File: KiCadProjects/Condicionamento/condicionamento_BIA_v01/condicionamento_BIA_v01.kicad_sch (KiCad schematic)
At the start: 33 parts, among them J2 tensoes, J3 sinais analogicos, J4 comunicacao / sinais digitais, U1 AD828AN, U2 AD828AN

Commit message: mudanças circuito de condicionamento
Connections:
- net +9V: now also U1.8 (V+), U2.8 (V+)
- net -9V: now also U1.4 (V-), U2.4 (V-)
- net Ampl1: now also U1.3 (+IN1), U2.3 (+IN1)
- net Ampl1_medida: now reaches C1.1, D1.2 (A), D2.1 (K), R1.2
- net Ampl1_medida: now also C2.1, D3.2 (A), D4.1 (K), R2.2
- net E1: now reaches U2.5 (+IN2)
- net E1: now also J3.1 (Pin_1)
- net E1_condicionado: now reaches C8.1, D7.2 (A), D8.1 (K), R12.2
- net E1_condicionado: now also J3.3 (Pin_3)
- net E2: now reaches J3.2 (Pin_2)
- net E2: now also U1.5 (+IN2)
- net E2_condicionado: now reaches J3.4 (Pin_4)
- net E2_condicionado: now also C7.1, D5.2 (A), D6.1 (K), R11.2
- removed net +12V: J2.2 (Pin_2), U1.8 (V+), U2.8 (V+)
- removed net -12V: J2.3 (Pin_3), U1.4 (V-), U2.4 (V-)
- new net VCC: J2.2 (Pin_2)
- new net VEE: J2.3 (Pin_3)

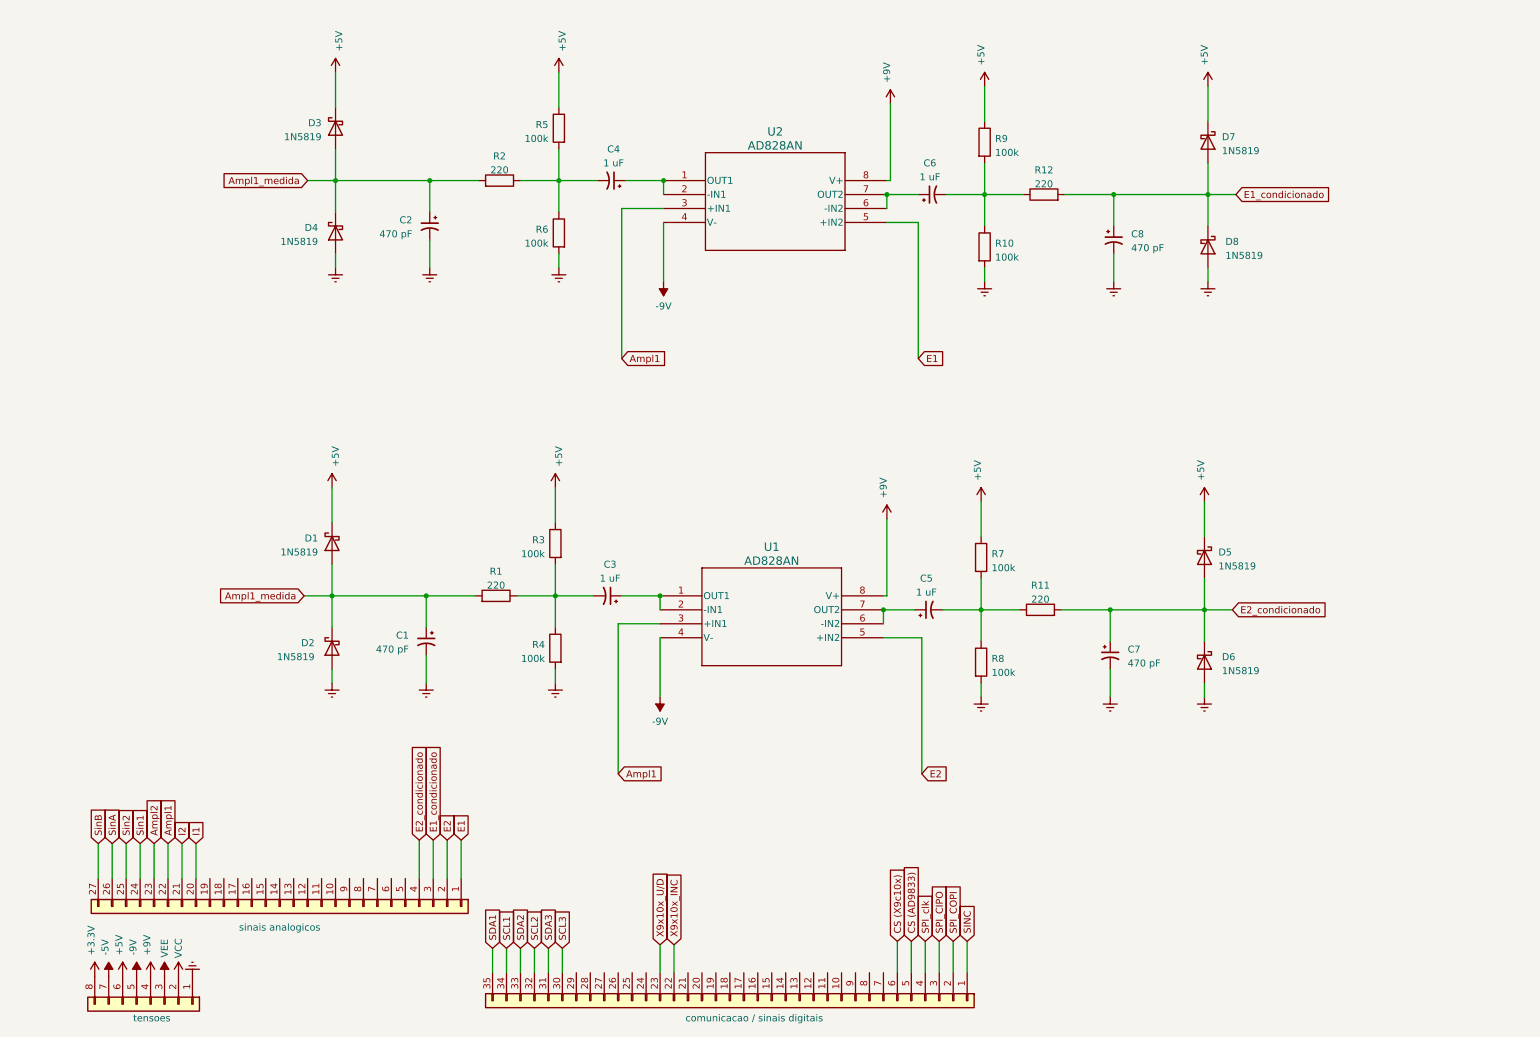
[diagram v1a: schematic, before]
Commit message: modificação: pinos de Vref para escolha da tensao de condicionamento
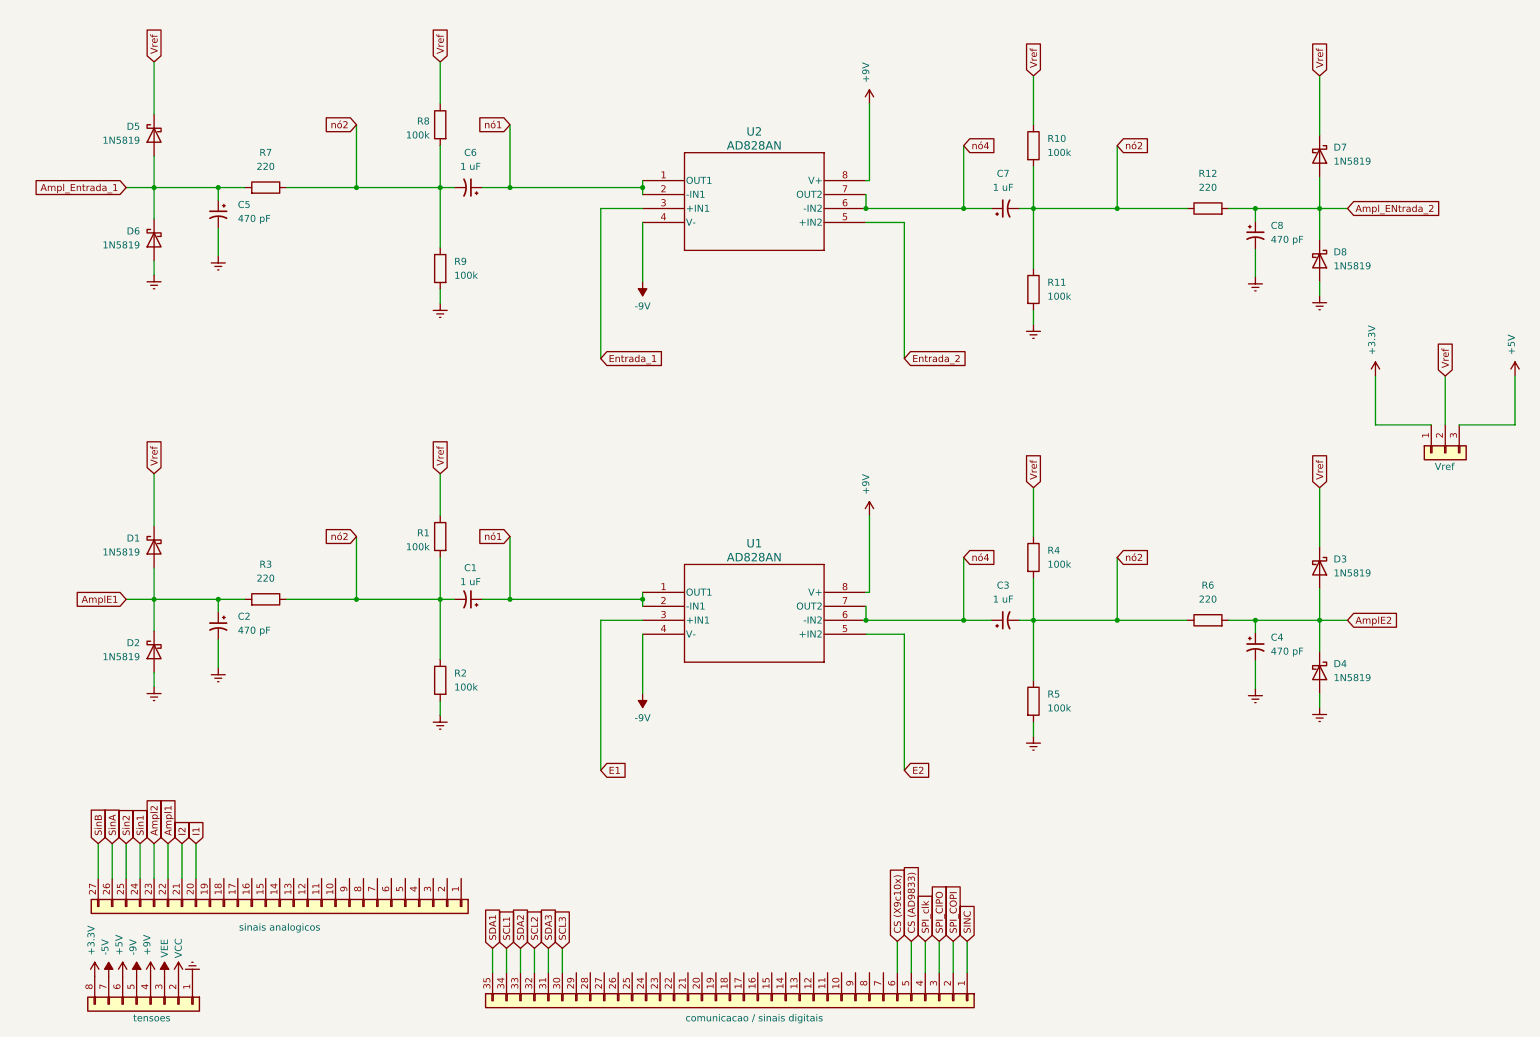
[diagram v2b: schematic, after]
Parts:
- added J1: Vref, Connector_PinHeader_2.54mm:PinHeader_1x03_P2.54mm_Vertical, symbol Connector_Generic:Conn_01x03
- C1, C7: value 470 pF -> 1 uF; footprint (none) -> Capacitor_THT:CP_Radial_D5.0mm_P2.50mm
- C2, C3, C6, C8: footprint (none) -> Capacitor_THT:CP_Radial_D5.0mm_P2.50mm
- C4, C5: value 1 uF -> 470 pF; footprint (none) -> Capacitor_THT:CP_Radial_D5.0mm_P2.50mm
- R1, R11, R2: value 220 -> 100k; footprint (none) -> Resistor_THT:R_Axial_DIN0207_L6.3mm_D2.5mm_P7.62mm_Horizontal
- R10, R12, R4, R5, R8, R9: footprint (none) -> Resistor_THT:R_Axial_DIN0207_L6.3mm_D2.5mm_P7.62mm_Horizontal
- R3, R6, R7: value 100k -> 220; footprint (none) -> Resistor_THT:R_Axial_DIN0207_L6.3mm_D2.5mm_P7.62mm_Horizontal
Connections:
- net +3.3V: now also J1.1 (Pin_1)
- net +5V: now also J1.3 (Pin_3); no longer D1.1 (K), D3.1 (K), D5.1 (K), D7.1 (K), R3.1, R5.1, R7.1, R9.1
- net Ampl1: no longer U1.3 (+IN1), U2.3 (+IN1)
- net E1: now also U1.3 (+IN1); no longer J3.1 (Pin_1), U2.5 (+IN2)
- net E2: no longer J3.2 (Pin_2)
- net Earth: now also C4.2, C5.2, R11.2, R2.2, R5.2, R9.2; no longer C1.2, C7.2, R10.2, R4.2, R6.2, R8.2
- net Vref: now reaches R1.1, R4.1
- net Vref: now also D1.1 (K), D3.1 (K), D5.1 (K), D7.1 (K), R10.1, R8.1, J1.2 (Pin_2); no longer C3.2, R3.2
- net nó2: now reaches C6.2, R12.1
- net nó2: now also C1.2, C3.2, C7.2, R1.2, R10.2, R11.1, R2.1, R3.1, R4.2, R5.1, R6.1, R7.1, R8.2, R9.1; no longer R10.1, R9.2
- net nó1: now reaches U2.1 (OUT1), U2.2 (-IN1)
- net nó1: now also C1.1, C6.1, U1.1 (OUT1), U1.2 (-IN1); no longer C4.1
- net nó4: now reaches U2.6 (-IN2), U2.7 (OUT2)
- net nó4: now also C3.1, C7.1, U1.6 (-IN2), U1.7 (OUT2); no longer C6.1
- removed net Ampl1_medida: C1.1, C2.1, D1.2 (A), D2.1 (K), D3.2 (A), D4.1 (K), R1.2, R2.2
- net E1_condicionado renamed Ampl_ENtrada_2
- net Ampl_ENtrada_2: no longer J3.3 (Pin_3)
- removed net E2_condicionado: C7.1, D5.2 (A), D6.1 (K), J3.4 (Pin_4), R11.2
- net X9x10x_INC: no longer names the net of J4.22 (Pin_22)
- net X9x10x_U/D: no longer names the net of J4.23 (Pin_23)
- new net AmplE1: C2.1, D1.2 (A), D2.1 (K), R3.2
- new net AmplE2: C4.1, D3.2 (A), D4.1 (K), R6.2
- new net Ampl_Entrada_1: C5.1, D5.2 (A), D6.1 (K), R7.2
- new net Entrada_1: U2.3 (+IN1)
- new net Entrada_2: U2.5 (+IN2)
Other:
- title: Barramento EITduino -> Condicionamento 2 canais duplicado
- moved on the sheet: U1

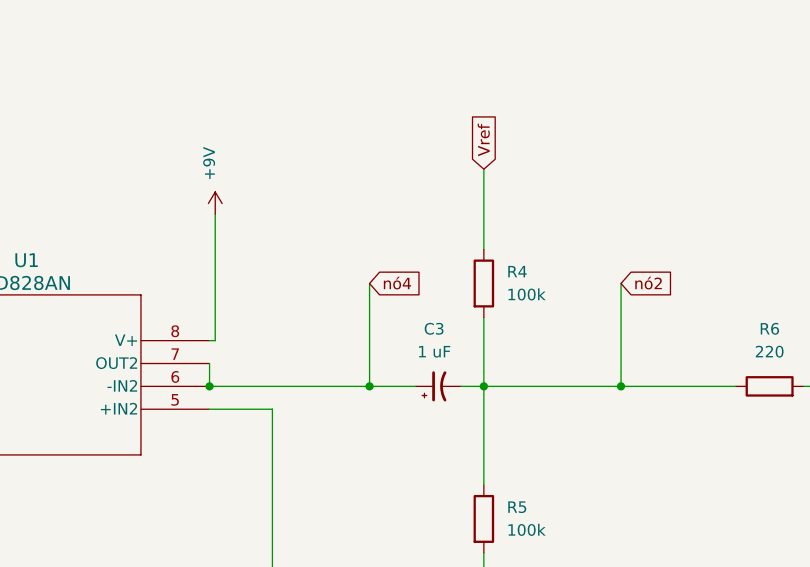
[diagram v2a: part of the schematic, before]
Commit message: modificação: pinos de Vref para escolha da tensao de condicionamento
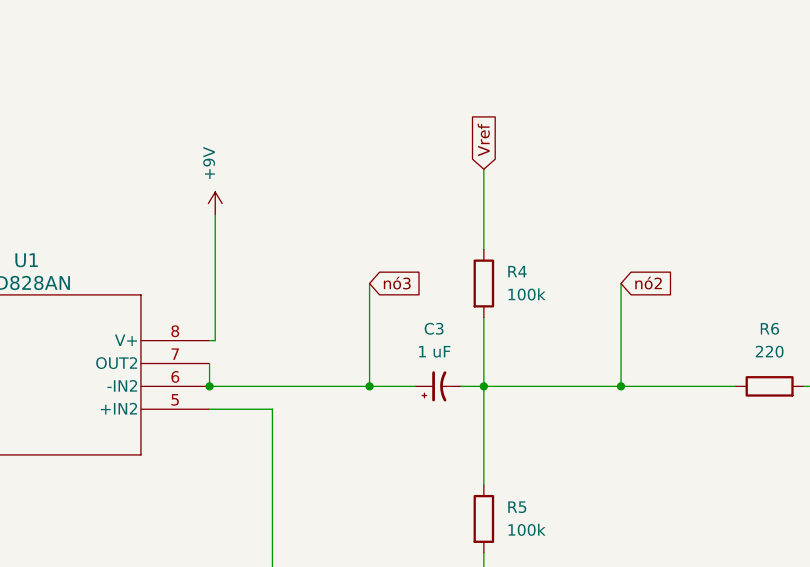
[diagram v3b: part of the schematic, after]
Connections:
- net nó4: no longer C3.1, U1.6 (-IN2), U1.7 (OUT2)
- new net nó3: C3.1, U1.6 (-IN2), U1.7 (OUT2)
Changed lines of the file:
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@@
     )
   )
-  (global_label "nó4" (shape input) (at 173.99 111.76 0) (fields_autoplaced)
+  (global_label "nó3" (shape input) (at 173.99 111.76 0) (fields_autoplaced)
     (effects (font (size 1.27 1.27)) (justify left))
     (property "Intersheetrefs" "${INTERSHEET_REFS}" (at 180.4033 111.76 0)

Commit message: reposicionamento do circuito
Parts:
- U1, U2: footprint N_8_ADI -> AD828AN:N_8_ADI
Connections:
- net nó1: no longer C6.1, U2.1 (OUT1), U2.2 (-IN1)
- net nó2: no longer C3.2, C6.2, C7.2, R10.2, R11.1, R12.1, R4.2, R5.1, R6.1, R7.1, R8.2, R9.1
- net nó4: now also C3.2, R4.2, R5.1, R6.1; no longer C7.1, U2.6 (-IN2), U2.7 (OUT2)
- new net nó5: C6.1, U2.1 (OUT1), U2.2 (-IN1)
- new net nó6: C6.2, R7.1, R8.2, R9.1
- new net nó7: C7.1, U2.6 (-IN2), U2.7 (OUT2)
- new net nó8: C7.2, R10.2, R11.1, R12.1
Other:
- moved on the sheet: C1, C2, C3, C4, C5, C6, C7, C8, D1, D2, D3, D4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

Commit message: condicionamento
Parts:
- removed C5, C8: 470 pF, Capacitor_THT:CP_Radial_D5.0mm_P2.50mm, symbol Device:C_Polarized_Small_US
- removed C6, C7: 1 uF, Capacitor_THT:CP_Radial_D5.0mm_P2.50mm, symbol Device:C_Polarized_Small_US
- removed D5, D6, D7, D8: 1N5819, Diode_THT:D_DO-41_SOD81_P10.16mm_Horizontal, symbol Diode:1N5819
- removed R10, R11, R9: 100k, Resistor_THT:R_Axial_DIN0207_L6.3mm_D2.5mm_P7.62mm_Horizontal, symbol Device:R
- removed R12: 220, Resistor_THT:R_Axial_DIN0207_L6.3mm_D2.5mm_P7.62mm_Horizontal, symbol Device:R
- removed U2: AD828AN, AD828AN:N_8_ADI, symbol AD828AN:AD828AN
- added Brd1: SSD1306, SSD1306:128x64OLED, symbol SSD1306-128x64_OLED:SSD1306
- added J5: sinais_condicionados, Connector_PinHeader_2.54mm:PinHeader_1x04_P2.54mm_Horizontal, symbol Connector_Generic:Conn_01x04
- added U2, U3: BluePill_STM32F103C, BluePill_breakouts:BluePill_STM32F103C, symbol bluepill_breakouts:BluePill_STM32F103C
- R7: value 220 -> 4k7
- R8: value 100k -> 4k7
- U1: footprint AD828AN:N_8_ADI -> footprints:N_8_ADI
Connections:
- net Ampl_Entrada_1 is gone; now on net +5V: R7.2
- net +5V: now also R8.2, Brd1.2 (VCC), U2.38 (5V_USB), U3.38 (5V_USB)
- net Earth: now also Brd1.1 (GND), U2.20 (GND), U3.20 (GND)
- net SCL1: now also R8.1, Brd1.3 (SCL), U2.34 (PB6_SCL1), U3.34 (PB6_SCL1)
- net SDA1: now also R7.1, Brd1.4 (SDA), U2.35 (PB7_SDA1), U3.35 (PB7_SDA1)
- net Vref: no longer R8.1
- net Ampl1 renamed AmpI1
- net AmpI1: now also J5.3 (Pin_3), J5.4 (Pin_4), U2.13 (PB0), U3.13 (PB0)
- net Ampl2 renamed AmpI2
- net AmplE1: no longer names the net of C2.1, D1.2 (A), D2.1 (K), R3.2
- net AmplE2 renamed Amp_E2
- net Amp_E2: now also J5.2 (Pin_2), U2.14 (PB1)
- removed net nó6: R7.1, R8.2
- new net Amp_E1: J5.1 (Pin_1), U3.14 (PB1)
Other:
- moved on the sheet: C1, C2, C3, C4, D1, D2, D3, D4, R1, R2, R3, R4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

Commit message: PCB
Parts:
- added J6: alimetacao_Master, Connector_PinHeader_2.54mm:PinHeader_1x02_P2.54mm_Vertical, symbol Connector_Generic:Conn_01x02
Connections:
- net +5V: now also J6.2 (Pin_2); no longer U3.38 (5V_USB)
- new net: J6.1 (Pin_1), U3.38 (5V_USB)
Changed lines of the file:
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@@
     (stroke (width 0) (type default))
   )
-  (wire (pts (xy 74.93 21.59) (xy 74.93 26.67))
+  (wire (pts (xy 74.93 13.97) (xy 74.93 26.67))
     (stroke (width 0) (type default))
   )
@@
     (stroke (width 0) (type default))
   )
+  (wire (pts (xy 60.96 13.97) (xy 64.77 13.97))
+    (stroke (width 0) (type default))
+  )
   (wire (pts (xy 95.25 158.75) (xy 95.25 165.1))
     (stroke (width 0) (type default))
@@
     (stroke (width 0) (type default))
   )
-  (wire (pts (xy 64.77 21.59) (xy 74.93 21.59))
-    (stroke (width 0) (type default))
-  )
   (wire (pts (xy 215.9 116.84) (xy 228.6 116.84))
     (stroke (width 0) (type default))
@@
   )
   (wire (pts (xy 252.73 92.71) (xy 252.73 103.505))
+    (stroke (width 0) (type default))
+  )
+  (wire (pts (xy 74.93 13.97) (xy 67.31 13.97))
     (stroke (width 0) (type default))
   )
@@
     )
   )
-  (symbol (lib_id "power:+5V") (at 64.77 21.59 90) (unit 1)
-    (in_bom yes) (on_board yes) (dnp no) (fields_autoplaced)
-    (property "Reference" "#PWR06" (at 68.58 21.59 0)
-      (effects (font (size 1.27 1.27)) hide)
-    )
-    (property "Value" "+5V" (at 60.96 21.59 90)
-      (effects (font (size 1.27 1.27)) (justify left))
-    )
-    (property "Footprint" "" (at 64.77 21.59 0)
-      (effects (font (size 1.27 1.27)) hide)
-    )
-    (property "Datasheet" "" (at 64.77 21.59 0)
+  (symbol (lib_id "power:+5V") (at 60.96 13.97 90) (unit 1)
+    (in_bom yes) (on_board yes) (dnp no) (fields_autoplaced)
+    (property "Reference" "#PWR06" (at 64.77 13.97 0)
+      (effects (font (size 1.27 1.27)) hide)
+    )
+    (property "Value" "+5V" (at 57.15 13.97 90)
+      (effects (font (size 1.27 1.27)) (justify left))
+    )
+    (property "Footprint" "" (at 60.96 13.97 0)
+      (effects (font (size 1.27 1.27)) hide)
+    )
+    (property "Datasheet" "" (at 60.96 13.97 0)
       (effects (font (size 1.27 1.27)) hide)
     )
@@
         )
       )
+    )
+  )
+  (symbol (lib_id "Connector_Generic:Conn_01x02") (at 67.31 19.05 270) (unit 1)
+    (in_bom yes) (on_board yes) (dnp no)
+    (property "Reference" "J6" (at 69.85 17.78 90)
+      (effects (font (size 1.27 1.27)) (justify left) hide)
+    )
+    (property "Value" "alimetacao_Master" (at 55.88 21.59 90)
+      (effects (font (size 1.27 1.27)) (justify left))
+    )
+    (property "Footprint" "Connector_PinHeader_2.54mm:PinHeader_1x02_P2.54mm_Vertical" (at 67.31 19.05 0)
+      (effects (font (size 1.27 1.27)) hide)
+    )
+    (property "Datasheet" "~" (at 67.31 19.05 0)
+      (effects (font (size 1.27 1.27)) hide)
+    )
+    (pin "1")
+    (pin "2")
+    (instances
+      (project "condicionamento_BIA_v01"
+        (path "/f0ff92cf-26e5-4ab9-977d-5f9689e8a5d0"
+          (reference "J6") (unit 1)
+        )
+      )

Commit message: PCB
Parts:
- added J7: Eletrodos, Connector_PinHeader_2.54mm:PinHeader_1x02_P2.54mm_Horizontal, symbol Connector_Generic:Conn_01x02
- U1: footprint footprints:N_8_ADI -> AD828:N_8_ADI
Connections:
- net Amp_E1: now also C2.1, D1.2 (A), D2.1 (K), R3.2
- net E1: now also J7.1 (Pin_1)
- net E2: now also J7.2 (Pin_2)
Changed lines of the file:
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@@
     )
   )
-  (global_label "Amp_E1" (shape input) (at 34.29 106.68 180) (fields_autoplaced)
+  (global_label "Amp_E1" (shape input) (at 35.56 113.03 180) (fields_autoplaced)
     (effects (font (size 1.27 1.27)) (justify right))
-    (property "Intersheetrefs" "${INTERSHEET_REFS}" (at 24.1272 106.68 0)
+    (property "Intersheetrefs" "${INTERSHEET_REFS}" (at 25.3972 113.03 0)
       (effects (font (size 1.27 1.27)) (justify right) hide)
     )
@@
     )
   )
+  (global_label "E2" (shape input) (at 31.75 151.13 90) (fields_autoplaced)
+    (effects (font (size 1.27 1.27)) (justify left))
+    (property "Intersheetrefs" "${INTERSHEET_REFS}" (at 31.75 145.8657 90)
+      (effects (font (size 1.27 1.27)) (justify right) hide)
+    )
+  )
   (global_label "Amp_E1" (shape input) (at 64.77 157.48 90) (fields_autoplaced)
     (effects (font (size 1.27 1.27)) (justify left))
@@
     (property "Intersheetrefs" "${INTERSHEET_REFS}" (at 222.3927 105.41 0)
       (effects (font (size 1.27 1.27)) (justify left) hide)
+    )
+  )
+  (global_label "E1" (shape input) (at 29.21 151.13 90) (fields_autoplaced)
+    (effects (font (size 1.27 1.27)) (justify left))
+    (property "Intersheetrefs" "${INTERSHEET_REFS}" (at 29.21 145.8657 90)
+      (effects (font (size 1.27 1.27)) (justify right) hide)
     )
   )
@@
       (effects (font (size 1.524 1.524)))
     )
-    (property "Footprint" "footprints:N_8_ADI" (at 129.54 111.76 0)
+    (property "Footprint" "AD828:N_8_ADI" (at 129.54 111.76 0)
       (effects (font (size 1.27 1.27) italic) hide)
     )
@@
         )
       )
+    )
+  )
+  (symbol (lib_id "Connector_Generic:Conn_01x02") (at 29.21 156.21 90) (mirror x) (unit 1)
+    (in_bom yes) (on_board yes) (dnp no)
+    (property "Reference" "J7" (at 26.67 154.94 90)
+      (effects (font (size 1.27 1.27)) (justify left) hide)
+    )
+    (property "Value" "Eletrodos" (at 34.29 160.02 90)
+      (effects (font (size 1.27 1.27)) (justify left))
+    )
+    (property "Footprint" "Connector_PinHeader_2.54mm:PinHeader_1x02_P2.54mm_Horizontal" (at 29.21 156.21 0)
+      (effects (font (size 1.27 1.27)) hide)
+    )
+    (property "Datasheet" "~" (at 29.21 156.21 0)
+      (effects (font (size 1.27 1.27)) hide)
+    )
+    (pin "1")
+    (pin "2")
+    (instances
+      (project "condicionamento_BIA_v01"
+        (path "/f0ff92cf-26e5-4ab9-977d-5f9689e8a5d0"
+          (reference "J7") (unit 1)
+        )
+      )

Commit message: PCB
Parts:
- Brd1: footprint SSD1306:128x64OLED -> OLED_i2c:128x64OLED
- U2, U3: footprint BluePill_breakouts:BluePill_STM32F103C -> STM32_Bluepill:BluePill_STM32F103C
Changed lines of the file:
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@@
       (effects (font (size 1.27 1.27)) (justify right))
     )
-    (property "Footprint" "BluePill_breakouts:BluePill_STM32F103C" (at 128.27 48.26 0)
+    (property "Footprint" "STM32_Bluepill:BluePill_STM32F103C" (at 128.27 48.26 0)
       (effects (font (size 1.27 1.27)) hide)
     )
@@
       (effects (font (size 1.27 1.27)) (justify left))
     )
-    (property "Footprint" "SSD1306:128x64OLED" (at 153.67 67.31 0)
+    (property "Footprint" "OLED_i2c:128x64OLED" (at 153.67 67.31 0)
       (effects (font (size 1.27 1.27)) hide)
     )
@@
       (effects (font (size 1.27 1.27)) (justify right))
     )
-    (property "Footprint" "BluePill_breakouts:BluePill_STM32F103C" (at 256.54 46.99 0)
-      (effects (font (size 1.27 1.27)) hide)
-    )
+    (property "Footprint" "STM32_Bluepill:BluePill_STM32F103C" (at 256.54 46.99 0)
+      (effects (font (size 1.27 1.27)) hide)
+    )
